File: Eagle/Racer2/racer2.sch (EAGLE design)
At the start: 9 parts

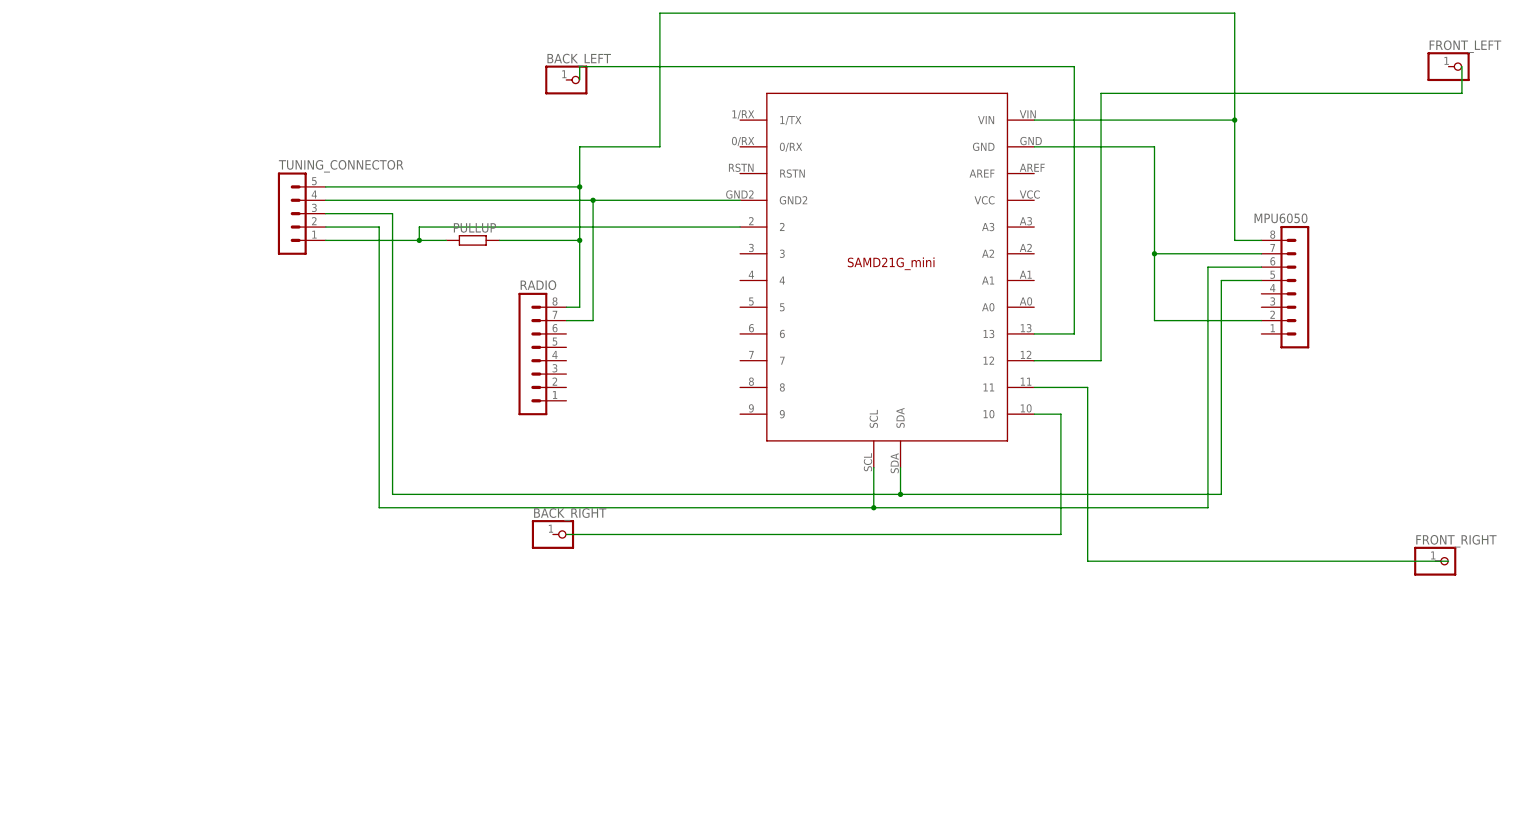
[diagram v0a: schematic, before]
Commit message: Changed structure of imu code.
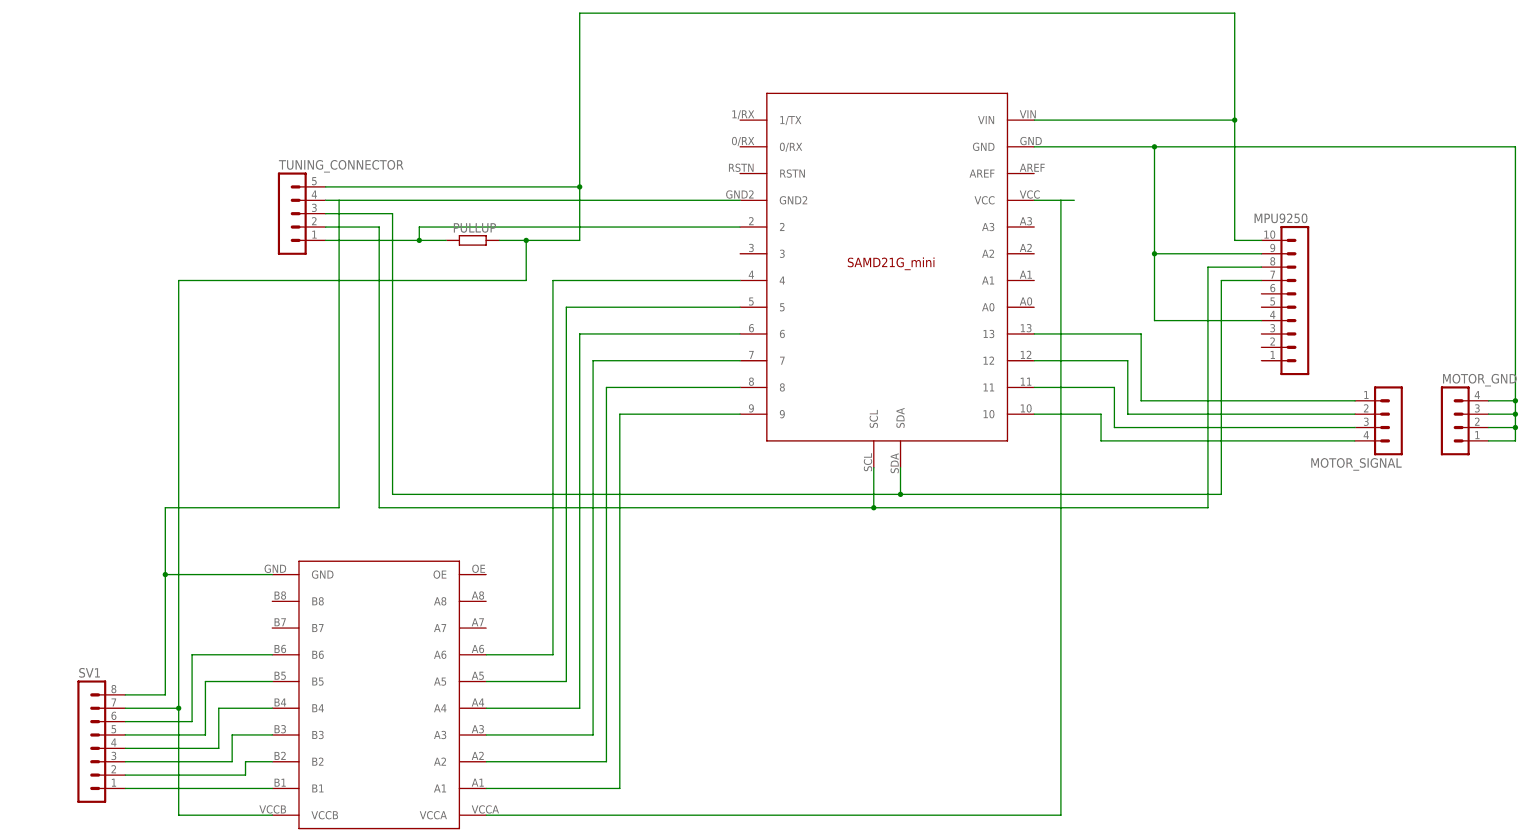
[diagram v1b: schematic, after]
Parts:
- removed BACK_LEFT, BACK_RIGHT, FRONT_LEFT, FRONT_RIGHT: (no value), adafruit:PINHD-1X1
- removed MPU6050, RADIO: (no value), con-lstb:MA08-1
- added MOTOR_GND, MOTOR_SIGNAL: (no value), con-lstb:MA04-1
- added MPU9250: (no value), con-lstb:MA10-1
- added SV1: (no value), con-lstb:MA08-1
- added U$2: LEVELSHIFT_8CH, quadcopter_comp:LEVELSHIFT_8CH
- U$1: device SAMD21_mini:SAMD21G_MINI -> quadcopter_comp:SAMD21G_MINI
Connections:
- new net N$10: MOTOR_SIGNAL.2, U$1.12
- new net N$11: SV1.4, U$2.B4
- new net N$12: MOTOR_SIGNAL.4, U$1.10
- new net N$13: SV1.5, U$2.B5
- new net N$14: SV1.6, U$2.B6
- new net N$18: U$1.VCC, U$2.VCCA
- new net N$19: U$1.4, U$2.A6
- new net N$20: U$1.5, U$2.A5
- new net N$21: U$1.6, U$2.A4
- new net N$22: U$1.7, U$2.A3
- new net N$23: U$1.8, U$2.A2
- new net N$24: U$1.9, U$2.A1
- new net N$9: MOTOR_SIGNAL.1, U$1.13
- net 5V: now also MPU9250.10, SV1.7, U$2.VCCB; no longer MPU6050.8, RADIO.8
- net GND2: now also SV1.8, U$2.GND; no longer RADIO.7
- net N$1: now also MPU9250.7; no longer MPU6050.5
- net N$2: now also MPU9250.8; no longer MPU6050.6
- net N$3: now also MOTOR_GND.1, MOTOR_GND.2, MOTOR_GND.3, MOTOR_GND.4, MPU9250.4, MPU9250.9; no longer MPU6050.2, MPU6050.7
- net N$4: now also SV1.1, U$2.B1; no longer U$1.10
- net N$5: now also MOTOR_SIGNAL.3
- net N$6: now also SV1.2, U$2.B2; no longer U$1.12
- net N$7: now also SV1.3, U$2.B3; no longer U$1.13

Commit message: Updated.
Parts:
- removed MOTOR_GND, MOTOR_SIGNAL: (no value), con-lstb:MA04-1
- removed MPU9250: (no value), con-lstb:MA10-1
- removed SV1: (no value), con-lstb:MA08-1
- added POWER: (no value), con-lstb:MA03-1
- added U$10, U$6, U$7, U$8, U$9: BRIDGE, quadcopter_comp:BRIDGE
- added U$3: FS_RADIO, quadcopter_comp:FS_RADIO
- added U$4: MPU9250, quadcopter_comp:MPU9250
- added U$5: MOTOR_HEADER, quadcopter_comp:MOTOR_HEADER
- U$1: value SAMD21G_MINI -> NANO; device quadcopter_comp:SAMD21G_MINI -> quadcopter_comp:NANO
- U$2: value LEVELSHIFT_8CH -> BUTTON_PULLUP; device quadcopter_comp:LEVELSHIFT_8CH -> quadcopter_comp:BUTTON_PULLUP
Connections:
- removed net GND2: SV1.8, TUNING_CONNECTOR.4, U$1.GND2, U$2.GND
- removed net N$20: U$1.5, U$2.A5
- removed net N$21: U$1.6, U$2.A4
- removed net N$22: U$1.7, U$2.A3
- removed net N$23: U$1.8, U$2.A2
- removed net N$24: U$1.9, U$2.A1
- new net GND: POWER.2, TUNING_CONNECTOR.4, U$1.GND, U$1.GND2, U$2.B, U$3.GND, U$4.AD0, U$4.GND, U$5.GND1, U$5.GND2, U$5.GND3, U$5.GND4
- new net N$15: U$3.VCC, U$9.A
- new net N$17: U$1.A4, U$6.A
- new net N$8: U$1.D6, U$3.CH5
- net 5V: now also POWER.3, U$1.5V, U$10.B, U$9.B; no longer MPU9250.10, SV1.7, U$1.VIN, U$2.VCCB
- net N$1: now also U$1.D12, U$8.A; no longer MPU9250.7, TUNING_CONNECTOR.3, U$1.SDA
- net N$10: now also U$1.D8, U$5.FL; no longer MOTOR_SIGNAL.2, U$1.12
- net N$11: now also U$1.D9, U$5.FR; no longer SV1.4, U$2.B4
- net N$12: now also U$1.D10, U$5.BL; no longer MOTOR_SIGNAL.4, U$1.10
- net N$13: now also U$1.D11, U$5.BR; no longer SV1.5, U$2.B5
- net N$14: now also U$2.A, U$3.BAT; no longer SV1.6, U$2.B6
- net N$16: now also U$8.B; no longer U$1.2
- net N$18: now also TUNING_CONNECTOR.2, U$4.SCL, U$7.B; no longer U$1.VCC, U$2.VCCA
- net N$19: now also U$10.A, U$4.VCC; no longer U$1.4, U$2.A6
- net N$2: now also U$1.A5, U$7.A; no longer MPU9250.8, TUNING_CONNECTOR.2, U$1.SCL
- net N$3: now also TUNING_CONNECTOR.3, U$4.SDA, U$6.B; no longer MOTOR_GND.1, MOTOR_GND.2, MOTOR_GND.3, MOTOR_GND.4, MPU9250.4, MPU9250.9, U$1.GND
- net N$4: now also U$1.D3, U$3.CH2; no longer SV1.1, U$2.B1
- net N$5: now also U$1.D2, U$3.CH1; no longer MOTOR_SIGNAL.3, U$1.11
- net N$6: now also U$1.D4, U$3.CH3; no longer SV1.2, U$2.B2
- net N$7: now also U$1.D5, U$3.CH4; no longer SV1.3, U$2.B3
- net N$9: now also U$1.D7, U$3.CH6; no longer MOTOR_SIGNAL.1, U$1.13

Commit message: Started on new Explorer code.
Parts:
- added PULLUP1: (no value), eagle-ltspice:R0204/7
- added U$11: ATMEGA328P, quadcopter_comp:ATMEGA328P
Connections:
- new net N$20: PULLUP1.2, U$11.PC6
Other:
- note added: "vdd"
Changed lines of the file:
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@@
 <setting verticaltext="up"/>
 </settings>
-<grid distance="0.1" unitdist="inch" unit="inch" style="lines" multiple="1" display="no" altdistance="0.01" altunitdist="inch" altunit="inch"/>
+<grid distance="0.1" unitdist="inch" unit="inch" style="lines" multiple="1" display="yes" altdistance="0.01" altunitdist="inch" altunit="inch"/>
 <layers>
 <layer number="1" name="Top" color="4" fill="1" visible="no" active="no"/>
@@
 <part name="U$9" library="quadcopter_comp" deviceset="BRIDGE" device=""/>
 <part name="U$10" library="quadcopter_comp" deviceset="BRIDGE" device=""/>
+<part name="U$11" library="quadcopter_comp" deviceset="ATMEGA328P" device=""/>
+<part name="PULLUP1" library="eagle-ltspice" deviceset="R" device="0204/7"/>
 </parts>
 <sheets>
 <sheet>
 <plain>
+<text x="-119.38" y="15.24" size="1.778" layer="91">vdd</text>
 </plain>
 <instances>
@@
 <instance part="U$9" gate="G$1" x="-2.54" y="81.28"/>
 <instance part="U$10" gate="G$1" x="109.22" y="63.5" rot="R90"/>
+<instance part="U$11" gate="G$1" x="-83.82" y="-7.62"/>
+<instance part="PULLUP1" gate="G$1" x="-109.22" y="15.24"/>
 </instances>
 <busses>
@@
 </segment>
 </net>
+<net name="N$20" class="0">
+<segment>
+<pinref part="PULLUP1" gate="G$1" pin="2"/>
+<pinref part="U$11" gate="G$1" pin="PC6"/>
+<wire x1="-104.14" y1="15.24" x2="-96.52" y2="15.24" width="0.1524" layer="91"/>
+</segment>
+</net>
